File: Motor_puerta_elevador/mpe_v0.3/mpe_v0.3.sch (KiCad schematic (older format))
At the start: 49 parts, among them J1 IBT2, J10 ENCODER, J11 Conn_01x04, J12 POWER, J13 MOTOR, J2 POWER, J3 MOTOR, J4 PROG, J5 IN1, J6 IN1, J7 IN1, J8 IN1, J9 IN1, P1 Power, P2 Analog, P3 Digital, P4 Digital, P6 CONN_01X01, P7 CONN_01X01, SW1 RESET, U1 ATmega3250PA-AU, U2 PC817, U3 PC817, U4 PC817, U5 PC817, U6 PC817, U7 DCDC_StepDown, Y1 16M

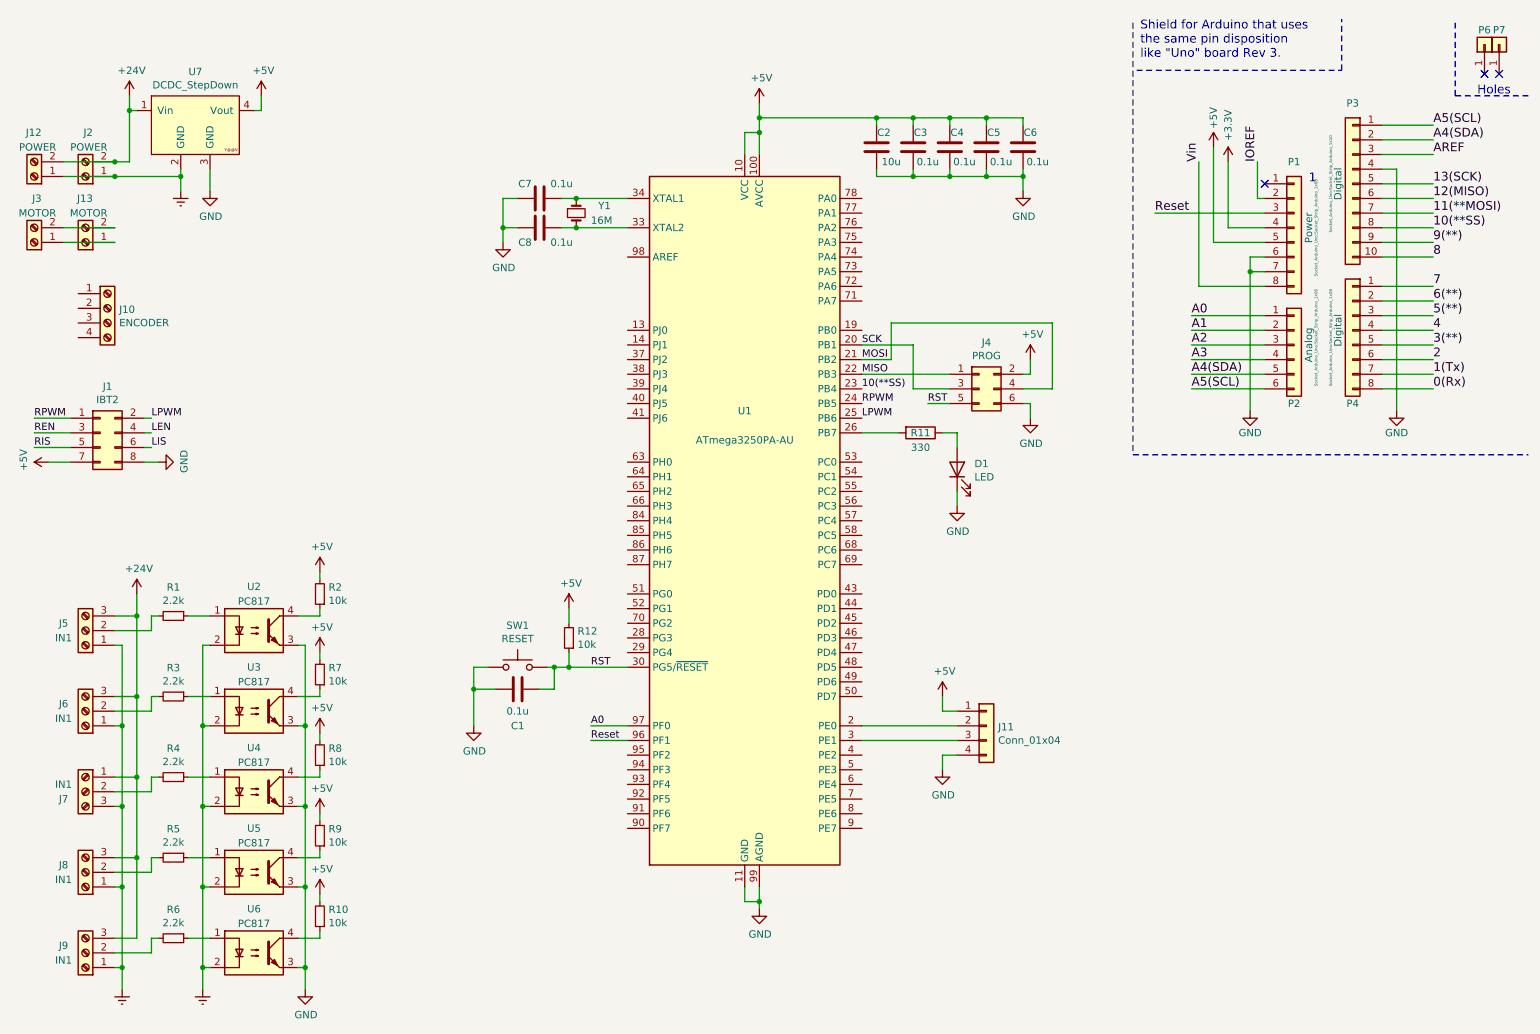
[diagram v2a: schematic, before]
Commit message: PCB todo cableado
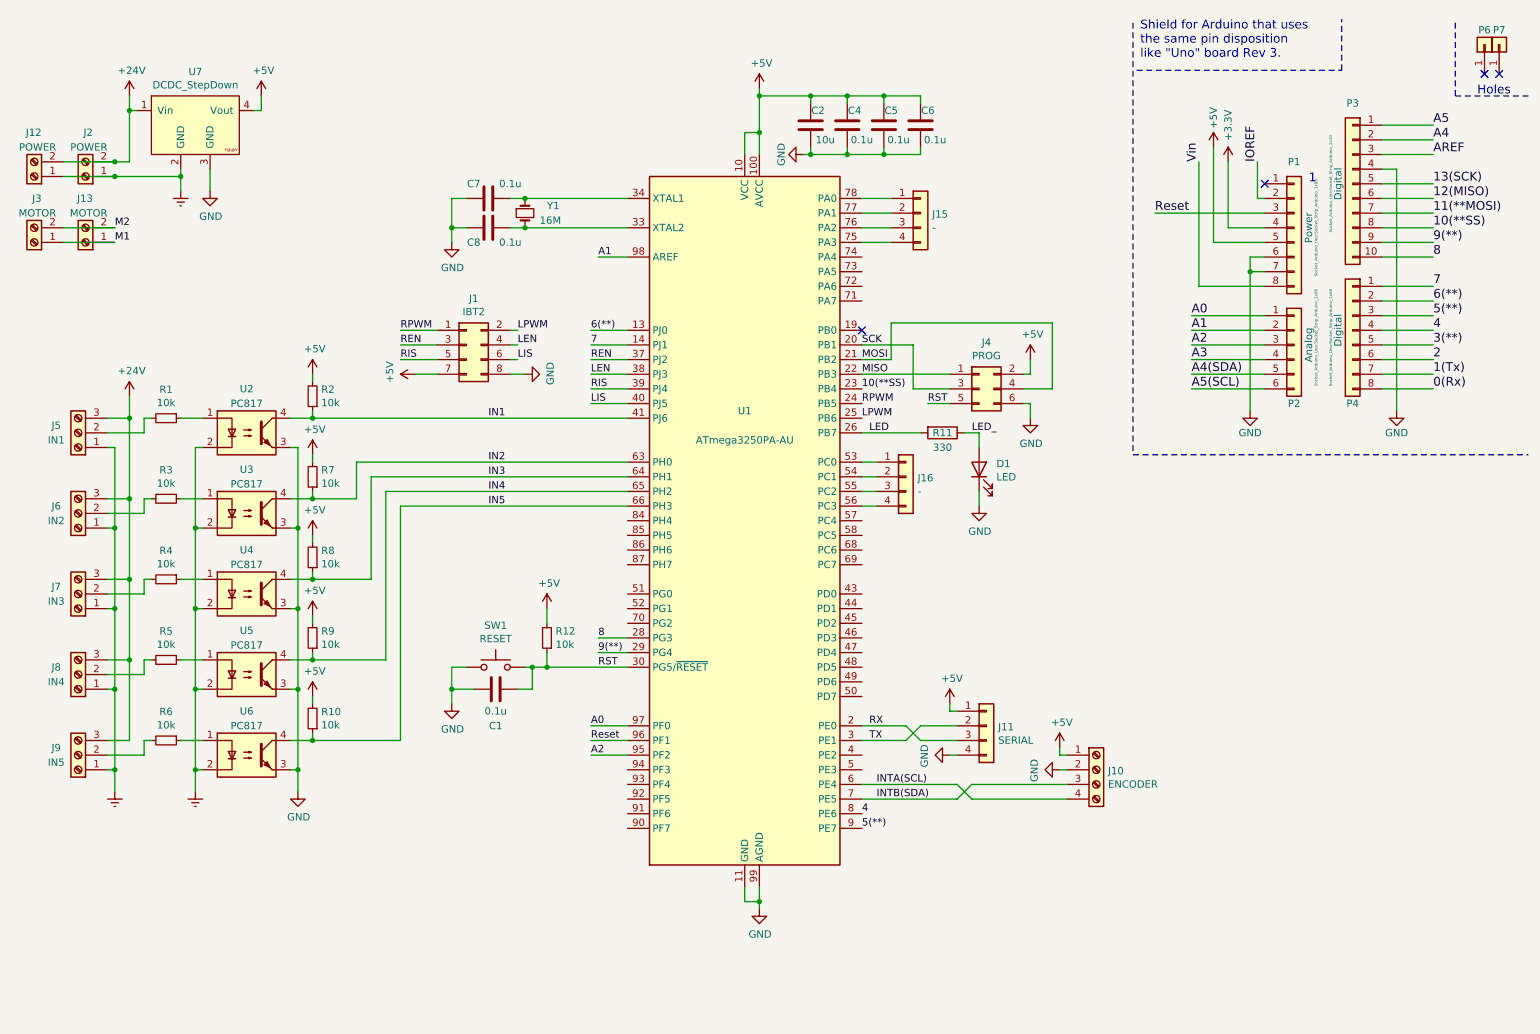
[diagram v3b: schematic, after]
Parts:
- removed C3: 0.1u, Capacitor_SMD:C_0805_2012Metric_Pad1.18x1.45mm_HandSolder, symbol Device:C
- added J15, J16: -, Connector_PinSocket_2.54mm:PinSocket_1x04_P2.54mm_Vertical, symbol Connector_Generic:Conn_01x04
- J11: value Conn_01x04 -> SERIAL
- J6: value IN1 -> IN2
- J7: value IN1 -> IN3
- J8: value IN1 -> IN4
- J9: value IN1 -> IN5
- R1, R3, R4, R5, R6: value 2.2k -> 10k
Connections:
- net +24V: now also J7.3 (Pin_3); no longer J7.1 (Pin_1)
- net +5V: now also J10.1 (Pin_1)
- net 4: now also U1.8 (PE6)
- net 5(**): now also U1.9 (PE7)
- net 6(**): now also U1.13 (PJ0)
- net 7: now also U1.14 (PJ1)
- net 8: now also U1.28 (PG3)
- net 9(**): now also U1.29 (PG4)
- net A1: now also U1.98 (AREF)
- net A2: now also U1.95 (PF2)
- net A4(SDA): no longer P3.2 (Pin_2)
- net A5(SCL): no longer P3.1 (Pin_1)
- net Earth: now also J7.1 (Pin_1); no longer J7.3 (Pin_3)
- net GND: now also J10.2 (Pin_2)
- net LEN: now also U1.38 (PJ3)
- net LIS: now also U1.40 (PJ5)
- net REN: now also U1.37 (PJ2)
- net RIS: now also U1.39 (PJ4)
- net RX: now reaches U1.2 (PE0)
- net RX: now also J11.3 (Pin_3); no longer J11.2 (Pin_2)
- net LED: now reaches R11.2, U1.26 (PB7)
- net TX: now reaches U1.3 (PE1)
- net TX: now also J11.2 (Pin_2); no longer J11.3 (Pin_3)
- net IN1: now reaches U1.41 (PJ6)
- net IN1: now also R2.1, U2.4
- net at U1.53 (PC0): now also J16.1 (Pin_1)
- net at U1.54 (PC1): now also J16.2 (Pin_2)
- net at U1.55 (PC2): now also J16.3 (Pin_3)
- net at U1.56 (PC3): now also J16.4 (Pin_4)
- net INTA(SCL): now reaches U1.6 (PE4)
- net INTA(SCL): now also J10.4 (Pin_4)
- net IN2: now reaches U1.63 (PH0)
- net IN2: now also R7.1, U3.4
- net IN3: now reaches U1.64 (PH1)
- net IN3: now also R8.1, U4.4
- net IN4: now reaches U1.65 (PH2)
- net IN4: now also R9.1, U5.4
- net IN5: now reaches U1.66 (PH3)
- net IN5: now also R10.1, U6.4
- net INTB(SDA): now reaches U1.7 (PE5)
- net INTB(SDA): now also J10.3 (Pin_3)
- net at U1.75 (PA3): now also J15.4 (Pin_4)
- net at U1.76 (PA2): now also J15.3 (Pin_3)
- net at U1.77 (PA1): now also J15.2 (Pin_2)
- net at U1.78 (PA0): now also J15.1 (Pin_1)
- net M1: now reaches J13.1 (Pin_1), J3.1 (Pin_1)
- net M2: now reaches J13.2 (Pin_2), J3.2 (Pin_2)
- net LED_: now reaches D1.2 (A), R11.1
- new net A4: P3.2 (Pin_2)
- new net A5: P3.1 (Pin_1)
- no-connect marks 3 -> 4
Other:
- moved on the sheet: C1, C2, C4, C5, C6, C7, C8, D1, J1, J10, J5, J6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

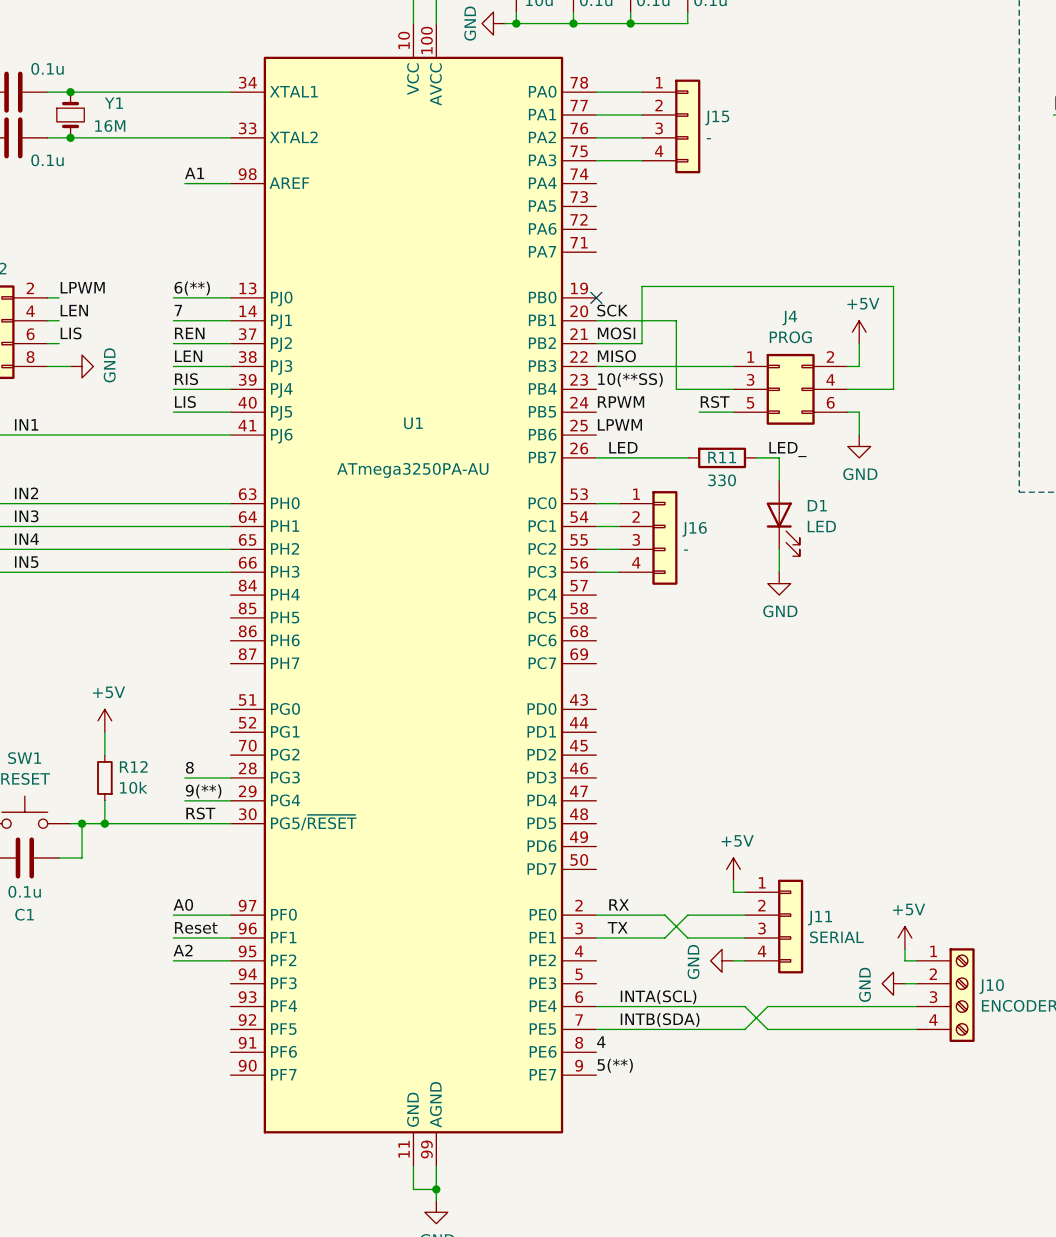
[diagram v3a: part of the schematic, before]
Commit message: reconectar entradas analógicas
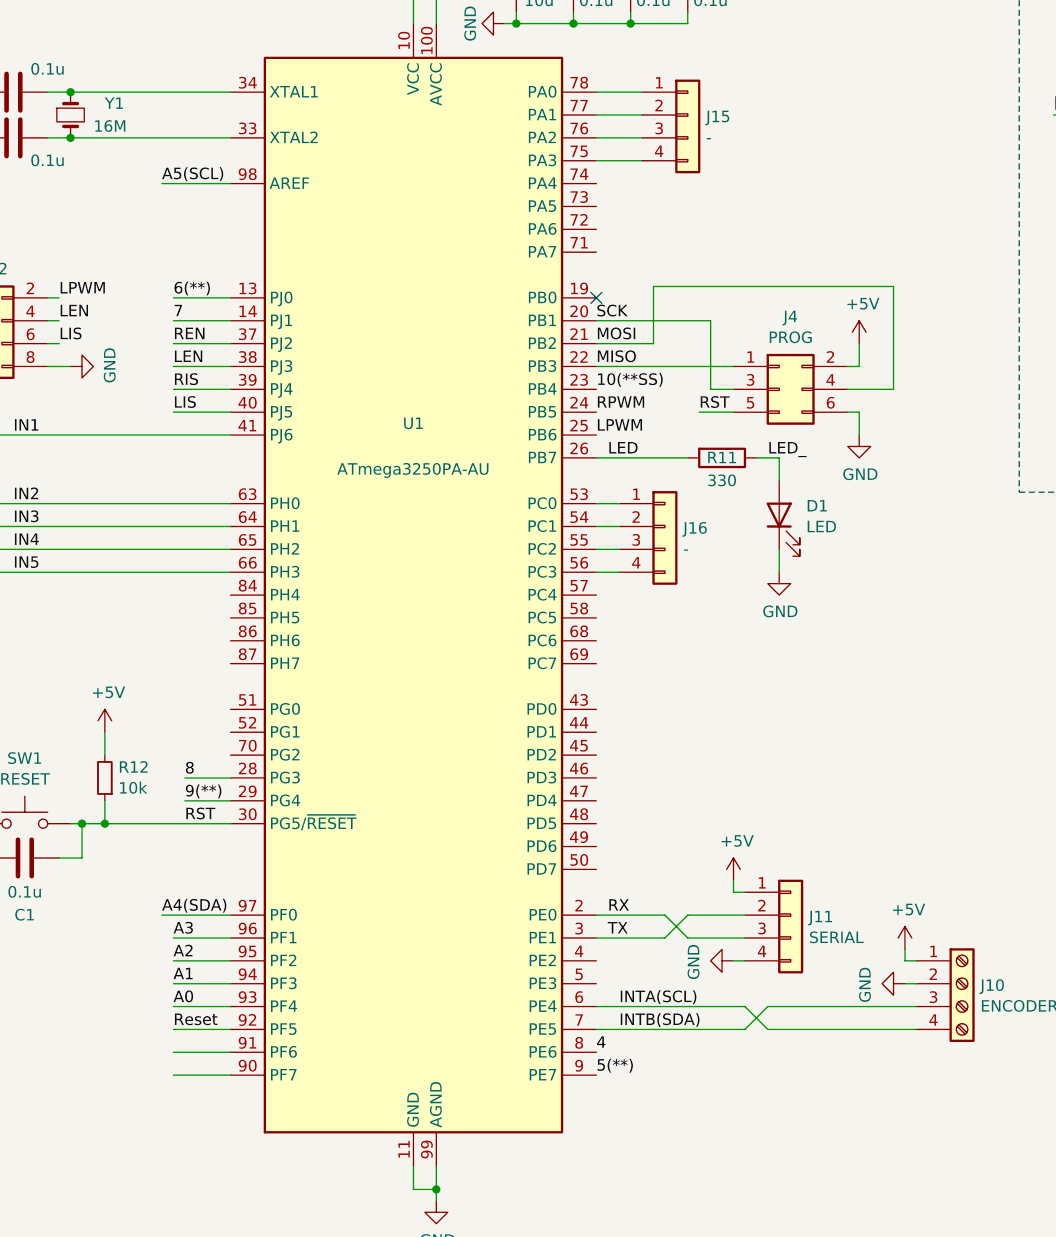
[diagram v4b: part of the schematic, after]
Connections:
- net A0: now also U1.93 (PF4); no longer U1.97 (PF0)
- net A1: now also U1.94 (PF3); no longer U1.98 (AREF)
- net A3: now also U1.96 (PF1)
- net A4(SDA): now also U1.97 (PF0)
- net A5(SCL): now also U1.98 (AREF)
- net Reset: now also U1.92 (PF5); no longer U1.96 (PF1)
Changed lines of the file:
@@
 	7250 2900 6650 2900
 Wire Wire Line
-	7000 2700 7000 3000
+	7150 2700 7150 3000
 Wire Wire Line
 	7800 2900 7750 2900
@@
 $EndComp
 Wire Wire Line
-	6850 2800 6850 2550
-Wire Wire Line
-	6850 2550 7950 2550
+	6900 2800 6900 2550
+Wire Wire Line
+	6900 2550 7950 2550
 Wire Wire Line
 	7950 2550 7950 3000
@@
 MOSI
 Wire Wire Line
-	7000 3000 7250 3000
-Wire Wire Line
-	6650 2800 6850 2800
+	7150 3000 7250 3000
+Wire Wire Line
+	6650 2800 6900 2800
 Text Label 6650 2700 0    50   ~ 0
 SCK
 Wire Wire Line
-	6650 2700 7000 2700
+	6650 2700 7150 2700
 $Comp
 L Device:R_Small R2
@@
 Text Label 4850 4900 0    50   ~ 0
 RST
-Text Label 4800 5300 0    50   ~ 0
-A0
+Text Label 4750 5300 0    50   ~ 0
+A4(SDA)
 Text Label 4800 5400 0    50   ~ 0
-Reset
-Wire Wire Line
-	4800 5300 5050 5300
+A3
+Wire Wire Line
+	4750 5300 5050 5300
 Wire Wire Line
 	5050 5400 4800 5400
@@
 	6650 3800 6750 3800
 Wire Wire Line
-	4850 2100 5050 2100
-Text Label 4850 2100 0    50   ~ 0
-A1
+	4750 2100 5050 2100
+Text Label 4750 2100 0    50   ~ 0
+A5(SCL)
 Wire Wire Line
 	5050 5500 4800 5500
 Text Label 4800 5500 0    50   ~ 0
 A2
+Wire Wire Line
+	5050 5600 4800 5600
+Wire Wire Line
+	5050 5700 4800 5700
+Wire Wire Line
+	5050 5800 4800 5800
+Wire Wire Line
+	5050 5900 4800 5900
+Wire Wire Line
+	5050 6000 4800 6000
+Text Label 4800 5600 0    50   ~ 0
+A1
+Text Label 4800 5700 0    50   ~ 0
+A0
+Text Label 4800 5800 0    50   ~ 0
+Reset
 $EndSCHEMATC
